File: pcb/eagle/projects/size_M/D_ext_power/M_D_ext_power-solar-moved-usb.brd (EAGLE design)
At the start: 30 parts

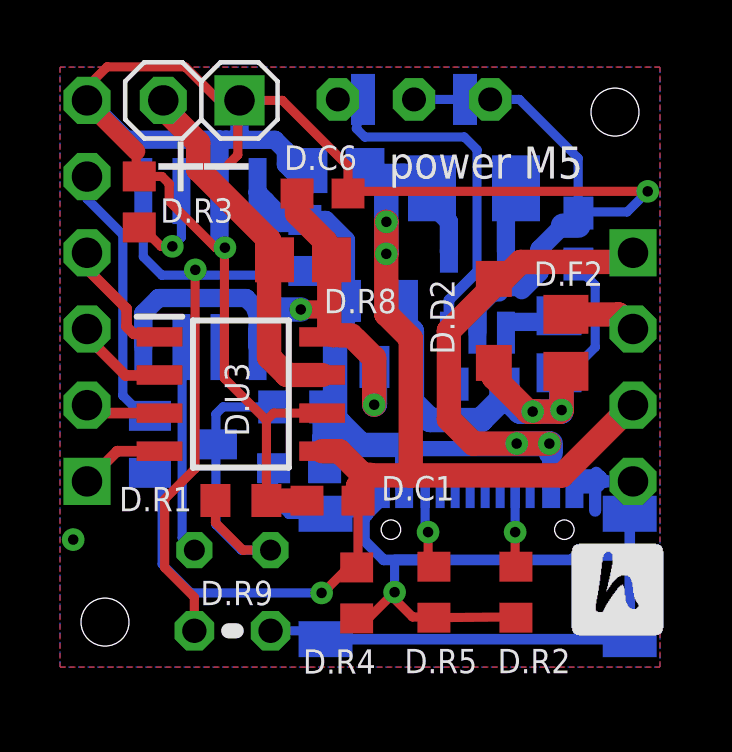
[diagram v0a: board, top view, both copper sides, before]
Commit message: LM3671_3.3 -> MCP1603T-330I attempt with  centered USB
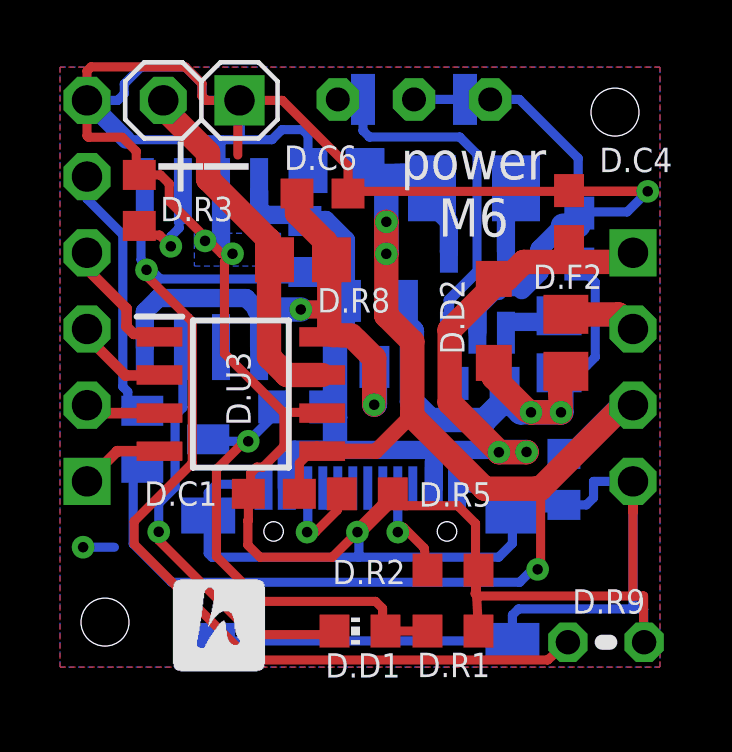
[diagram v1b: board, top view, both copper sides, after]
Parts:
- D.D1: value LED_1.8 -> (none); device hugo:LED_1.8 -> led:CHIP-LED0603
- moved D.R9 12.5 mm to (18.7, 1.33)
- moved D.C4 12.3 mm to (17.5, 15.5), flipped to the top, turned to 270 degrees
- moved D.R1 8.30 mm to (13.6, 1.70)
- moved D.R4 7.88 mm to (17.3, 6.76), flipped to the bottom
- moved D.D1 4.83 mm to (10.5, 1.70), flipped to the top, turned to 90 degrees
- moved D.R5 3.96 mm to (10.7, 6.28), turned to 0 degrees
- moved U$1 3.91 mm to (10.5, 2.64)
- moved D.R2 2.22 mm to (13.6, 3.73), turned to 0 degrees
- moved D.C1 1.97 mm to (7.63, 6.28)
- moved D.T2 0.31 mm to (4.34, 8.09)
- moved U$2 0.05 mm to (5.23, 13.8)
- moved D.R3 0.05 mm to (3.14, 16.1)
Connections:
- net N$3: now also D.D1.C1; no longer D.D1.1
- net PA3: now also D.D1.A1; no longer D.D1.2
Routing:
- net GND: track 122.8 -> 159.9 mm, vias 4 -> 5
- net N$8: track 20.9 -> 35.4 mm
- net VCC: track 45.4 -> 53.5 mm
- net N$3: track 6.95 -> 14.3 mm, vias 0 -> 1
- net PA3: track 10.9 -> 16.1 mm, vias 0 -> 1
- net VUSB: track 40.6 -> 36.8 mm
- net N$6: track 2.68 -> 3.44 mm
- net N$4: track 2.80 -> 3.39 mm
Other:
- board text added: "power M6"
- board text removed: "power M5"
